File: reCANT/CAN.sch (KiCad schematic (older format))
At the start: 15 parts, among them J3 Screw_Terminal_01x04, U4 MCP2558FD-xSN, U5 MCP2558FD-xSN, U6 74LVC1G66, U7 74LVC1G66

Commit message: Add LCSC part numbers for each component. Not that chipocalypse makes building this right now feasible...
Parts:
- C16, C17, C18, C19: LCSC (none) -> C49678
- R10, R11: LCSC (none) -> C17673
- R8, R9: LCSC (none) -> C17437
- U4, U5: LCSC (none) -> C124015
- U6, U7: LCSC (none) -> C97489
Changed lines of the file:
@@
 F 3 "" H 3000 6250 30  0000 C CNN
 F 4 "MCR03ERTF1200" H 3000 6250 60  0001 C CNN "MPN"
+F 5 "C17437" V 3000 6250 50  0001 C CNN "LCSC"
 	1    3000 6250
 	0    1    1    0
@@
 F 2 "Package_TO_SOT_SMD:SOT-353_SC-70-5_Handsoldering" H 9650 1300 50  0001 C CNN
 F 3 "http://www.ti.com/lit/sg/scyt129e/scyt129e.pdf" H 9650 1300 50  0001 C CNN
+F 4 "C97489" H 9650 1300 50  0001 C CNN "LCSC"
 	1    9650 1300
 	1    0    0    -1
@@
 F 3 "" H 9400 1850 30  0000 C CNN
 F 4 "MCR03ERTF5100" H 9400 1850 60  0001 C CNN "MPN"
+F 5 "C17673" V 9400 1850 50  0001 C CNN "LCSC"
 	1    9400 1850
 	1    0    0    -1
@@
 F 3 "" H 1500 6200 30  0000 C CNN
 F 4 "MCR03ERTF1200" H 1500 6200 60  0001 C CNN "MPN"
+F 5 "C17437" V 1500 6200 50  0001 C CNN "LCSC"
 	1    1500 6200
 	0    1    1    0
@@
 F 2 "Package_SO:SOIC-8_3.9x4.9mm_P1.27mm" H 4150 3600 50  0001 C CNN
 F 3 "https://ww1.microchip.com/downloads/en/DeviceDoc/20005533A.pdf" H 4150 4200 50  0001 C CNN
+F 4 "C124015" H 4150 4200 50  0001 C CNN "LCSC"
 	1    4150 4200
 	1    0    0    -1
@@
 F 2 "Package_SO:SOIC-8_3.9x4.9mm_P1.27mm" H 1800 3550 50  0001 C CNN
 F 3 "https://ww1.microchip.com/downloads/en/DeviceDoc/20005533A.pdf" H 1800 4150 50  0001 C CNN
+F 4 "C124015" H 1800 4150 50  0001 C CNN "LCSC"
 	1    1800 4150
 	1    0    0    -1
@@
 F 2 "Package_TO_SOT_SMD:SOT-353_SC-70-5_Handsoldering" H 7750 1350 50  0001 C CNN
 F 3 "http://www.ti.com/lit/sg/scyt129e/scyt129e.pdf" H 7750 1350 50  0001 C CNN
+F 4 "C97489" H 7750 1350 50  0001 C CNN "LCSC"
 	1    7750 1350
 	1    0    0    -1
@@
 F 3 "" H 7500 1900 30  0000 C CNN
 F 4 "MCR03ERTF5100" H 7500 1900 60  0001 C CNN "MPN"
+F 5 "C17673" V 7500 1900 50  0001 C CNN "LCSC"
 	1    7500 1900
 	1    0    0    -1
@@
 F 2 "Capacitor_SMD:C_0805_2012Metric" H 1050 4550 50  0001 C CNN
 F 3 "~" H 1050 4550 50  0001 C CNN
+F 4 "C49678" H 1050 4550 50  0001 C CNN "LCSC"
 	1    1050 4550
 	1    0    0    -1
@@
 F 2 "Capacitor_SMD:C_0805_2012Metric" H 2550 3750 50  0001 C CNN
 F 3 "~" H 2550 3750 50  0001 C CNN
+F 4 "C49678" V 2550 3750 50  0001 C CNN "LCSC"
 	1    2550 3750
 	0    1    1    0
@@
 F 2 "Capacitor_SMD:C_0805_2012Metric" H 4850 3800 50  0001 C CNN
 F 3 "~" H 4850 3800 50  0001 C CNN
+F 4 "C49678" V 4850 3800 50  0001 C CNN "LCSC"
 	1    4850 3800
 	0    1    1    0
@@
 F 2 "Capacitor_SMD:C_0805_2012Metric" H 3300 4600 50  0001 C CNN
 F 3 "~" H 3300 4600 50  0001 C CNN
+F 4 "C49678" H 3300 4600 50  0001 C CNN "LCSC"
 	1    3300 4600
 	1    0    0    -1

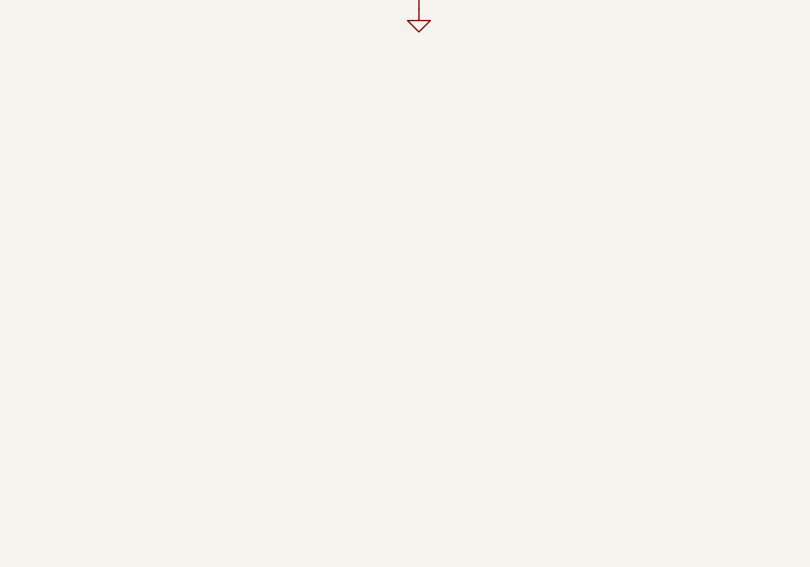
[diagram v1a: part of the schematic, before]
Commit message: Added test points for debugging USB. Fixed impedence on USB traces to be correct for JLCPCBs JLC7628 buildup
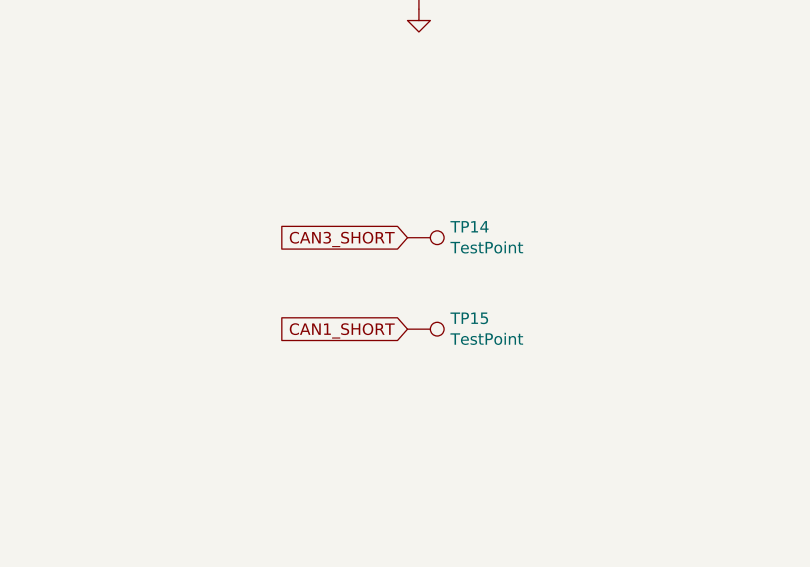
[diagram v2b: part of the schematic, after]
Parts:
- added TP14, TP15: TestPoint, TestPoint:TestPoint_Pad_D1.0mm, symbol Connector:TestPoint
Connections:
- net CAN1_SHORT: now also TP15.1
- net CAN3_SHORT: now also TP14.1
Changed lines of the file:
@@
 	1    0    0    -1
 $EndComp
+Text GLabel 7450 3150 0    50   Input ~ 0
+CAN3_SHORT
+Text GLabel 7450 3550 0    50   Input ~ 0
+CAN1_SHORT
+$Comp
+L Connector:TestPoint TP14
+U 1 1 623338B5
+P 7450 3150
+F 0 "TP14" V 7404 3338 50  0000 L CNN
+F 1 "TestPoint" V 7495 3338 50  0000 L CNN
+F 2 "TestPoint:TestPoint_Pad_D1.0mm" H 7650 3150 50  0001 C CNN
+F 3 "~" H 7650 3150 50  0001 C CNN
+	1    7450 3150
+	0    1    1    0
+$EndComp
+$Comp
+L Connector:TestPoint TP15
+U 1 1 623340D2
+P 7450 3550
+F 0 "TP15" V 7404 3738 50  0000 L CNN
+F 1 "TestPoint" V 7495 3738 50  0000 L CNN
+F 2 "TestPoint:TestPoint_Pad_D1.0mm" H 7650 3550 50  0001 C CNN
+F 3 "~" H 7650 3550 50  0001 C CNN
+	1    7450 3550
+	0    1    1    0
+$EndComp
 $EndSCHEMATC
